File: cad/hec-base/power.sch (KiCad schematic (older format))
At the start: 54 parts, among them IC201 LMR14206, IC202 LTC3406ES5, IC203 74LVC1G57, IC204 TPS3307-33, IC205 STM32F103C8Tx

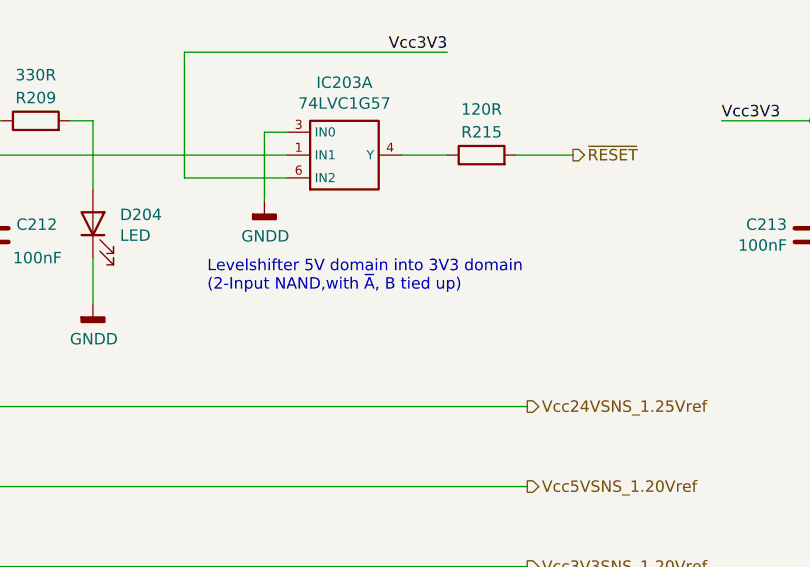
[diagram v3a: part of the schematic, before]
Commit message: Alle in-akzeptablen DRC-Fehler im Layout behoben.
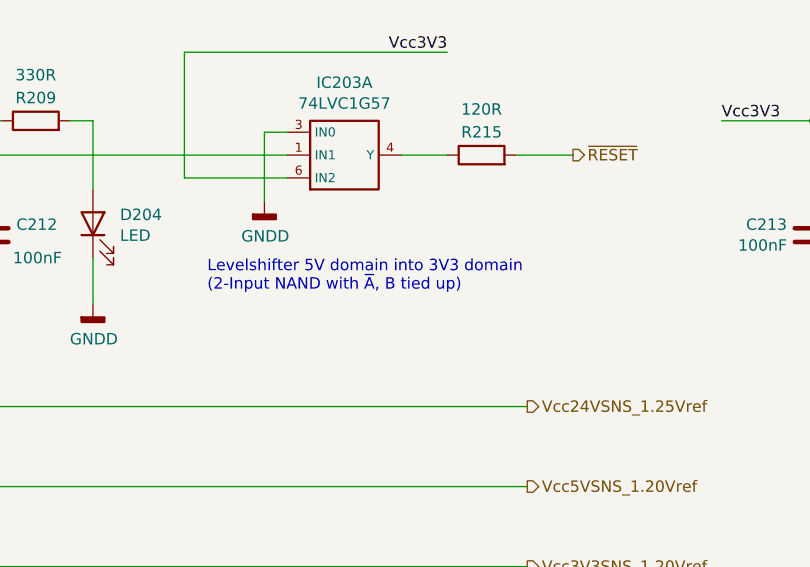
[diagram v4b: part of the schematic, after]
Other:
- note added: "Levelshifter 5V domain into 3V3 domain\n(2-Input NAND with ~A~, B tied up)"
- note removed: "Levelshifter 5V domain into 3V3 domain\n(2-Input NAND,with ~A~, B tied up)"
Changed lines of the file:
@@
 Vcc3V3
 Text Notes 7150 7400 0    50   ~ 0
-Levelshifter 5V domain into 3V3 domain\n(2-Input NAND,with ~A~, B tied up)
+Levelshifter 5V domain into 3V3 domain\n(2-Input NAND with ~A~, B tied up)
 $Comp
 L Device:R R215

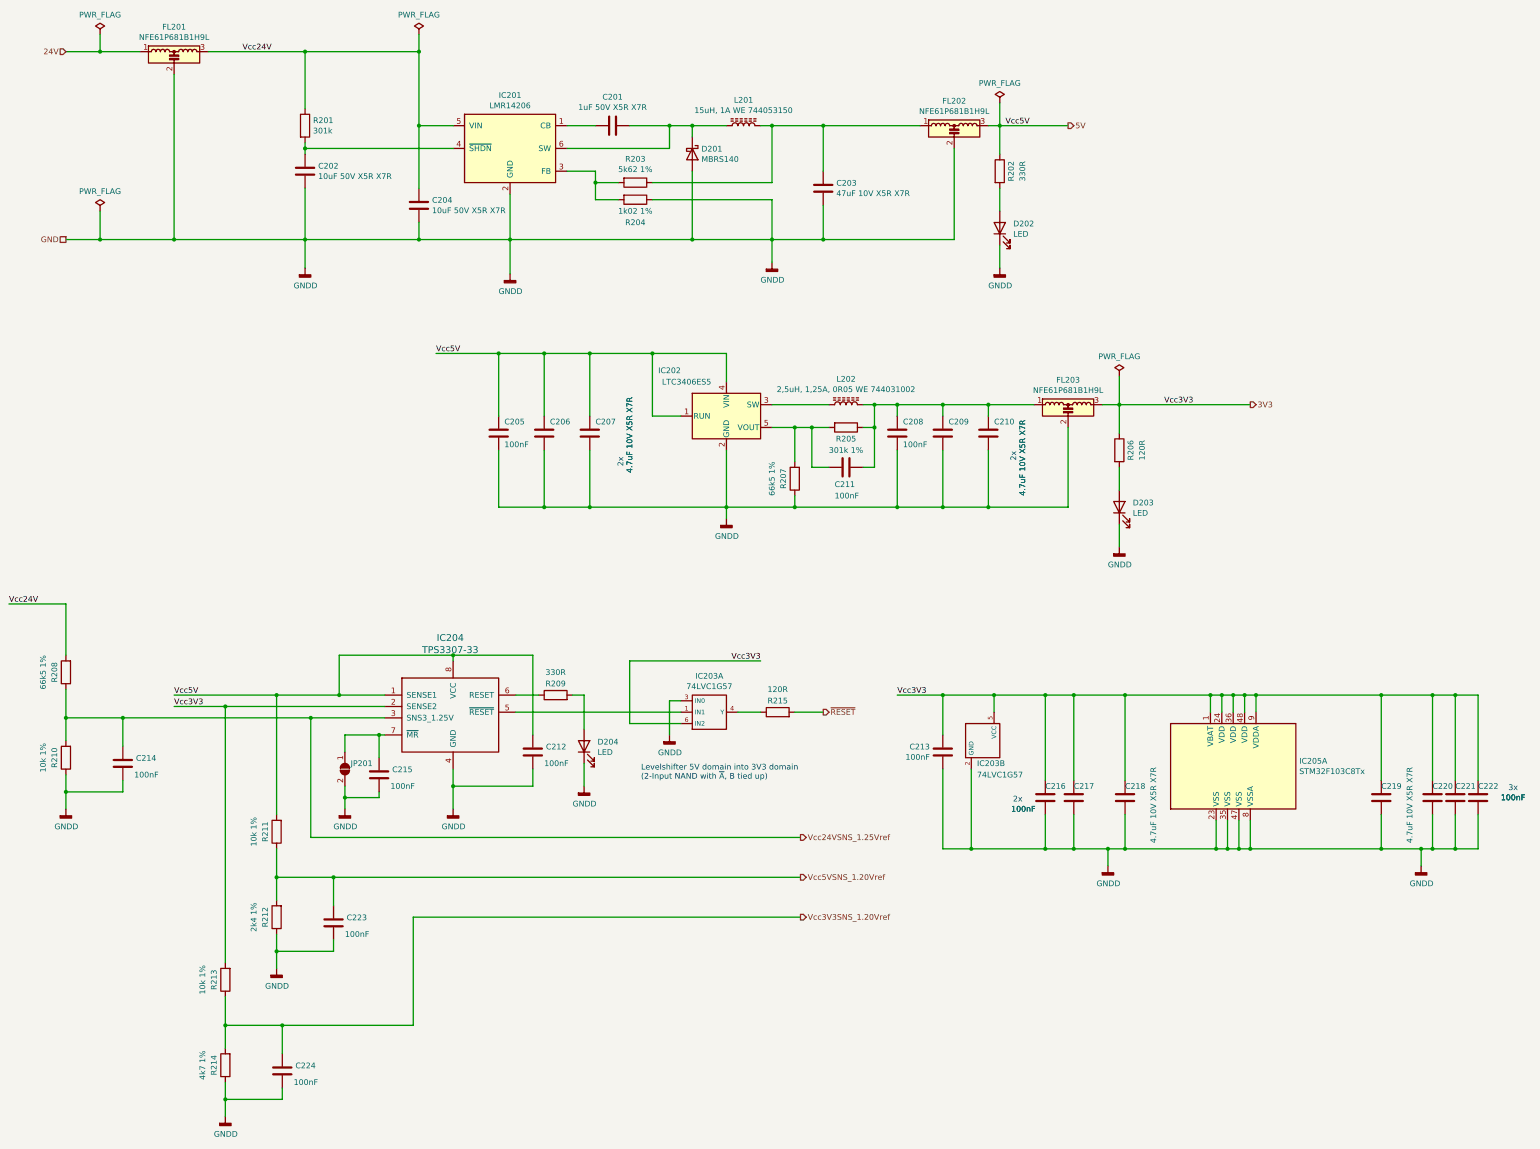
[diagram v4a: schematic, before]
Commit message: Texte für Silkscreen und Bestückungsplan platziert.
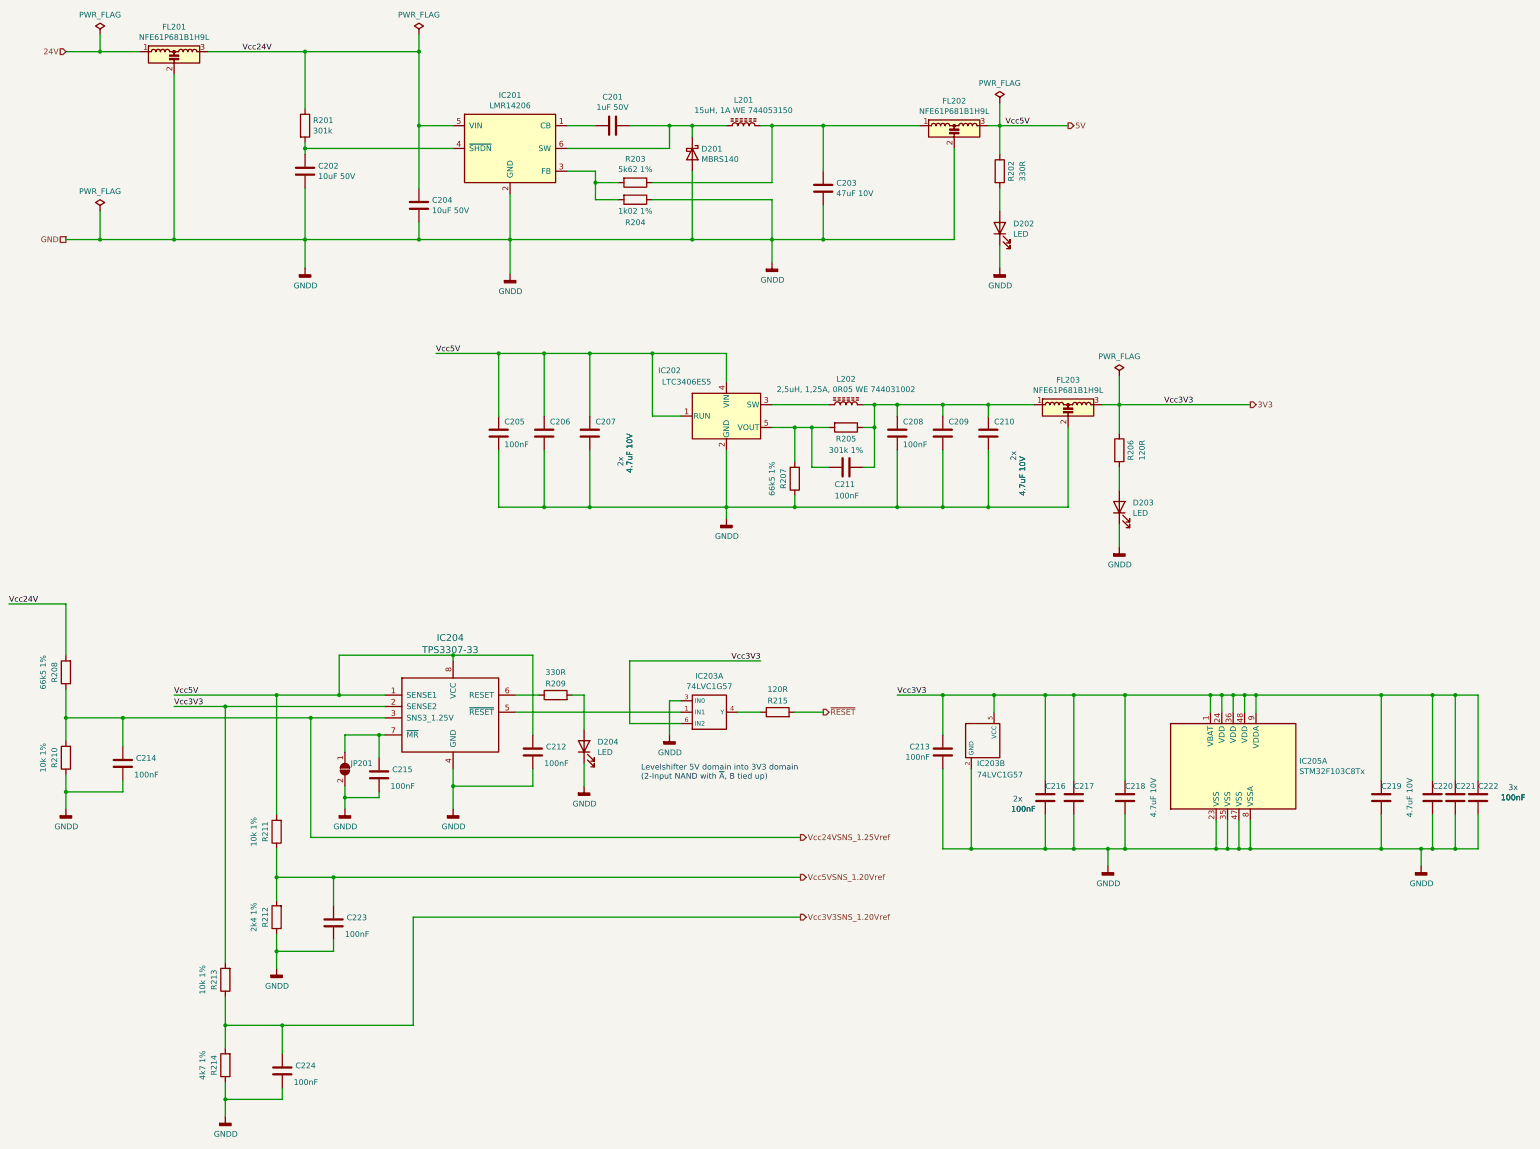
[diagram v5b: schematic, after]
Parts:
- C201: value 1uF 50V X5R X7R -> 1uF 50V
- C202, C204: value 10uF 50V X5R X7R -> 10uF 50V
- C203: value 47uF 10V X5R X7R -> 47uF 10V
- C206, C207, C209, C210, C218, C219: value 4.7uF 10V X5R X7R -> 4.7uF 10V
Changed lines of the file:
@@
 P 5200 2350
 F 0 "C204" H 5315 2396 50  0000 L CNN
-F 1 "10uF 50V X5R X7R" H 5315 2305 50  0000 L CNN
+F 1 "10uF 50V" H 5315 2305 50  0000 L CNN
 F 2 "Capacitor_SMD:C_1206_3216Metric" H 5238 2200 50  0001 C CNN
 F 3 "~" H 5200 2350 50  0001 C CNN
@@
 P 8750 2200
 F 0 "C203" H 8865 2246 50  0000 L CNN
-F 1 "47uF 10V X5R X7R" H 8865 2155 50  0000 L CNN
+F 1 "47uF 10V" H 8865 2155 50  0000 L CNN
 F 2 "Capacitor_SMD:C_1210_3225Metric" H 8788 2050 50  0001 C CNN
 F 3 "~" H 8750 2200 50  0001 C CNN
@@
 P 6900 1650
 F 0 "C201" V 6648 1650 50  0000 C CNN
-F 1 "1uF 50V X5R X7R" V 6739 1650 50  0000 C CNN
+F 1 "1uF 50V" V 6739 1650 50  0000 C CNN
 F 2 "Capacitor_SMD:C_0805_2012Metric" H 6938 1500 50  0001 C CNN
 F 3 "~" H 6900 1650 50  0001 C CNN
@@
 P 6700 4350
 F 0 "C207" H 6650 4250 50  0000 R CNN
-F 1 "4.7uF 10V X5R X7R" V 6350 4700 50  0000 R CNN
+F 1 "4.7uF 10V" V 6350 4700 50  0000 R CNN
 F 2 "Capacitor_SMD:C_0805_2012Metric" H 6738 4200 50  0001 C CNN
 F 3 "~" H 6700 4350 50  0001 C CNN
@@
 P 6300 4350
 F 0 "C206" H 6250 4250 50  0000 R CNN
-F 1 "4.7uF 10V X5R X7R" V 5550 4700 50  0000 R CNN
+F 1 "4.7uF 10V" V 5550 4700 50  0000 R CNN
 F 2 "Capacitor_SMD:C_0805_2012Metric" H 6338 4200 50  0001 C CNN
 F 3 "~" H 6300 4350 50  0001 C CNN
@@
 P 10200 4350
 F 0 "C210" H 10150 4250 50  0000 R CNN
-F 1 "4.7uF 10V X5R X7R" V 9900 4900 50  0000 R CNN
+F 1 "4.7uF 10V" V 9900 4900 50  0000 R CNN
 F 2 "Capacitor_SMD:C_0805_2012Metric" H 10238 4200 50  0001 C CNN
 F 3 "~" H 10200 4350 50  0001 C CNN
@@
 P 9800 4350
 F 0 "C209" H 9750 4250 50  0000 R CNN
-F 1 "4.7uF 10V X5R X7R" V 9100 4900 50  0000 R CNN
+F 1 "4.7uF 10V" V 9100 4900 50  0000 R CNN
 F 2 "Capacitor_SMD:C_0805_2012Metric" H 9838 4200 50  0001 C CNN
 F 3 "~" H 9800 4350 50  0001 C CNN
@@
 P 11400 7550
 F 0 "C218" H 11400 7450 50  0000 R CNN
-F 1 "4.7uF 10V X5R X7R" V 11150 7950 50  0000 R CNN
+F 1 "4.7uF 10V" V 11150 7550 50  0000 C CNN
 F 2 "Capacitor_SMD:C_0805_2012Metric" H 11438 7400 50  0001 C CNN
 F 3 "~" H 11400 7550 50  0001 C CNN
@@
 P 13650 7550
 F 0 "C219" H 13650 7450 50  0000 R CNN
-F 1 "4.7uF 10V X5R X7R" V 13400 7950 50  0000 R CNN
+F 1 "4.7uF 10V" V 13400 7550 50  0000 C CNN
 F 2 "Capacitor_SMD:C_0805_2012Metric" H 13688 7400 50  0001 C CNN
 F 3 "~" H 13650 7550 50  0001 C CNN
@@
 P 4200 2050
 F 0 "C202" H 4085 2004 50  0000 R CNN
-F 1 "10uF 50V X5R X7R" H 4085 2095 50  0000 R CNN
+F 1 "10uF 50V" H 4085 2095 50  0000 R CNN
 F 2 "Capacitor_SMD:C_1206_3216Metric" H 4238 1900 50  0001 C CNN
 F 3 "~" H 4200 2050 50  0001 C CNN
